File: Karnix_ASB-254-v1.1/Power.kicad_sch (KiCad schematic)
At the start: 37 parts, among them Q1 AO3401A, U1 ST1S14, U2 TLV62565DBVT, U3 RS3236-2.5YF5, U4 RS3236-3.3YF5

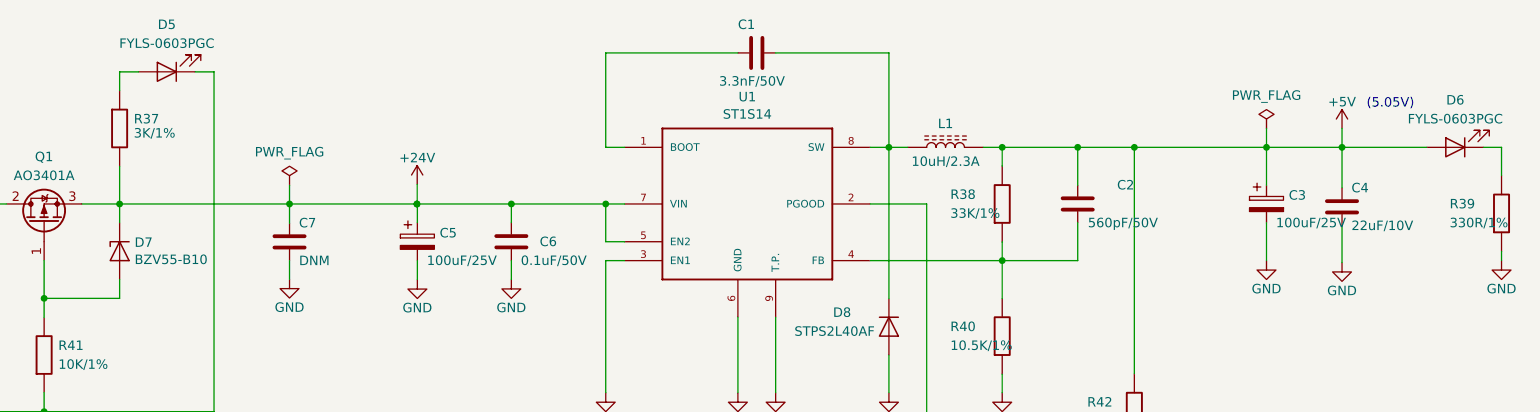
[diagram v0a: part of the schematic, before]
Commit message: Increase current limiting resistors for LEDs lower brightness
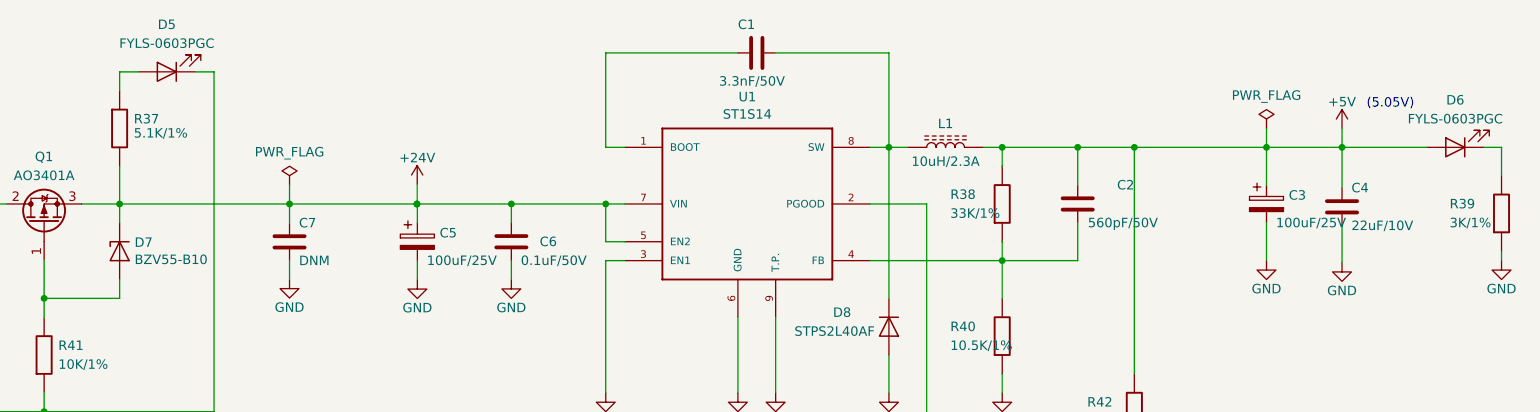
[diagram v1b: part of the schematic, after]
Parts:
- R37: value 3K/1% -> 5.1K/1%; Mfr. Part Number RC0402FR-073KL -> RC0402FR-075K1L
- R39: value 330R/1% -> 3K/1%; Mfr. Part Number RC0402FR-07330RL -> RC0402FR-073KL
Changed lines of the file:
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@@
       (effects (font (size 1.27 1.27)) (justify left))
     )
-    (property "Value" "3K/1%" (at 139.446 52.197 90)
+    (property "Value" "5.1K/1%" (at 139.446 52.197 90)
       (effects (font (size 1.27 1.27)) (justify left))
     )
@@
       (effects (font (size 1.27 1.27)) hide)
     )
-    (property "Mfr. Part Number" "RC0402FR-073KL" (at 137.541 51.562 0)
+    (property "Mfr. Part Number" "RC0402FR-075K1L" (at 137.541 51.562 0)
       (effects (font (size 1.27 1.27)) hide)
     )
@@
       (effects (font (size 1.27 1.27)) (justify left))
     )
-    (property "Value" "330R/1%" (at 316.484 64.262 90)
+    (property "Value" "3K/1%" (at 316.484 64.262 90)
       (effects (font (size 1.27 1.27)) (justify left))
     )
@@
       (effects (font (size 1.27 1.27)) hide)
     )
-    (property "Mfr. Part Number" "RC0402FR-07330RL" (at 323.469 62.992 0)
-      (effects (font (size 1.27 1.27)) hide)
-    )
+    (property "Mfr. Part Number" "RC0402FR-073KL" (at 323.469 62.992 0)
+      (effects (font (size 1.27 1.27)) hide)
+    )
